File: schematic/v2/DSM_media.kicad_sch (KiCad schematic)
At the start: 3 parts, among them J22 USB_A

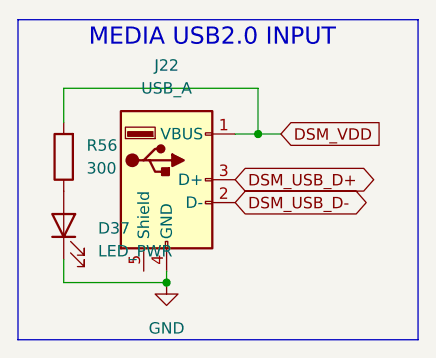
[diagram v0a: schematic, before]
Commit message: v2 updates. remove sniffer
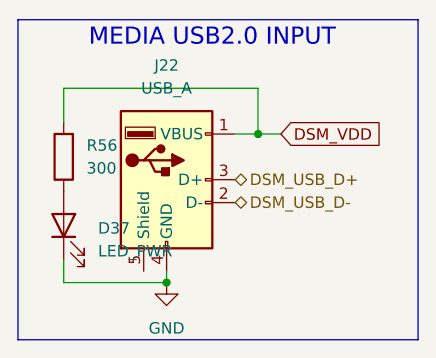
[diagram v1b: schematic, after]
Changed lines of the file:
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@@
 		)
 	)
-	(global_label "DSM_USB_D-"
+	(hierarchical_label "DSM_USB_D-"
 		(shape bidirectional)
 		(at 149.86 97.79 0)
-		(fields_autoplaced yes)
 		(effects
 			(font
@@
 			(justify left)
 		)
-		(property "Intersheetrefs" "${INTERSHEET_REFS}"
-			(at 166.1727 97.79 0)
-			(effects
-				(font
-					(size 1.27 1.27)
-				)
-				(justify left)
-				(hide yes)
-			)
-		)
 	)
-	(global_label "DSM_USB_D+"
+	(hierarchical_label "DSM_USB_D+"
 		(shape bidirectional)
 		(at 149.86 95.25 0)
-		(fields_autoplaced yes)
 		(effects
 			(font
@@
 			(justify left)
 		)
-		(property "Intersheetrefs" "${INTERSHEET_REFS}"
-			(at 166.1727 95.25 0)
-			(effects
-				(font
-					(size 1.27 1.27)
-				)
-				(justify left)
-				(hide yes)
-			)
-		)
 	)

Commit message: no errors in the ERC!
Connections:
- no-connect marks 0 -> 1
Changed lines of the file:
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@@
 		(color 0 0 0 0)
+	)
+	(no_connect
+		(at 139.7 105.41)
 	)
 	(wire
